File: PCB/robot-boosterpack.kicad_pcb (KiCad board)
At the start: 2 copper layers, 60 x 100 mm, 61 parts, among them IC1 DRV8833, IC2 TPS77033, IC3 TPS77050, IC4 LMR61428, J1 3.3V, J2 5V, J3 9V, M1 MOTOR, M2 MOTOR

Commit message: moved battery connector
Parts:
- moved CONN2 49.1 mm to (176.9, 131.8), turned to 90 degrees
- moved R5 4.41 mm to (195.4, 85.9), turned to 0 degrees
- moved J1 0.28 mm to (183.4, 144.4)
- moved J2 0.28 mm to (178.5, 144.4)
- moved D2 0.22 mm to (178.4, 152.2)
- moved R10 0.21 mm to (205.8, 106.7)
- moved D3 0.20 mm to (173.5, 152.2)
- moved D1 0.10 mm to (183.4, 152.2)
- moved R16 0.07 mm to (183.4, 149.1)
- moved R17 0.06 mm to (178.4, 149.1)
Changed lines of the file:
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@@
   )
   (module SM0603 (layer F.Cu)
-    (at 173.435 149.125 90)
+    (at 173.4 149.1 90)
     (attr smd)
     (fp_text reference R18 (at 0 0 90) (layer F.SilkS)
@@
   )
   (module SM0603 (layer B.Cu)
-    (at 205.75 106.5 270)
+    (at 205.8 106.7 270)
     (attr smd)
     (fp_text reference R10 (at 0 0 270) (layer B.SilkS)
@@
   )
   (module SM0603 (layer F.Cu)
-    (at 183.467 149.125 90)
+    (at 183.4 149.1 90)
     (attr smd)
     (fp_text reference R16 (at 0 0 90) (layer F.SilkS)
@@
   )
   (module SM0603 (layer F.Cu)
-    (at 178.451 149.125 90)
+    (at 178.4 149.1 90)
     (attr smd)
     (fp_text reference R17 (at 0 0 90) (layer F.SilkS)
@@
   )
   (module SM0603 (layer B.Cu)
-    (at 199.25 83.75 180)
-    (attr smd)
-    (fp_text reference R5 (at 0 0 180) (layer B.SilkS)
-      (effects (font (size 0.508 0.4572) (thickness 0.1143)) (justify mirror))
-    )
-    (fp_text value 22k (at 0 0 180) (layer B.SilkS) hide
-      (effects (font (size 0.508 0.4572) (thickness 0.1143)) (justify mirror))
-    )
-    (fp_line (start -1.143 0.635) (end 1.143 0.635) (layer B.SilkS) (width 0.127))
-    (fp_line (start 1.143 0.635) (end 1.143 -0.635) (layer B.SilkS) (width 0.127))
-    (fp_line (start 1.143 -0.635) (end -1.143 -0.635) (layer B.SilkS) (width 0.127))
-    (fp_line (start -1.143 -0.635) (end -1.143 0.635) (layer B.SilkS) (width 0.127))
-    (pad 1 smd rect (at -0.762 0 180) (size 0.635 1.143)
+    (at 195.4 85.9)
+    (attr smd)
+    (fp_text reference R5 (at 0 0) (layer B.SilkS)
+      (effects (font (size 0.508 0.4572) (thickness 0.1143)) (justify mirror))
+    )
+    (fp_text value 22k (at 0 0) (layer B.SilkS) hide
+      (effects (font (size 0.508 0.4572) (thickness 0.1143)) (justify mirror))
+    )
+    (fp_line (start -1.143 0.635) (end 1.143 0.635) (layer B.SilkS) (width 0.127))
+    (fp_line (start 1.143 0.635) (end 1.143 -0.635) (layer B.SilkS) (width 0.127))
+    (fp_line (start 1.143 -0.635) (end -1.143 -0.635) (layer B.SilkS) (width 0.127))
+    (fp_line (start -1.143 -0.635) (end -1.143 0.635) (layer B.SilkS) (width 0.127))
+    (pad 1 smd rect (at -0.762 0) (size 0.635 1.143)
       (layers B.Cu B.Paste B.Mask)
       (net 1 +3.3V)
     )
-    (pad 2 smd rect (at 0.762 0 180) (size 0.635 1.143)
+    (pad 2 smd rect (at 0.762 0) (size 0.635 1.143)
       (layers B.Cu B.Paste B.Mask)
       (net 24 N-0000021)
@@
   )
   (module PIN_ARRAY_3X1 (layer F.Cu)
-    (at 173.435 143.125 90)
+    (at 173.4 143.1 90)
     (descr "Connecteur 3 pins")
     (tags "CONN DEV")
@@
   )
   (module PIN_ARRAY_2X1 (layer F.Cu)
-    (at 178.451 144.125 90)
+    (at 178.5 144.4 90)
     (descr "Connecteurs 2 pins")
     (tags "CONN DEV")
@@
   )
   (module PIN_ARRAY_2X1 (layer F.Cu)
-    (at 226 131.5 270)
+    (at 176.9 131.8 90)
     (descr "Connecteurs 2 pins")
     (tags "CONN DEV")
-    (fp_text reference CONN2 (at 0 -1.905 270) (layer F.SilkS) hide
+    (fp_text reference CONN2 (at 0 -1.905 90) (layer F.SilkS) hide
       (effects (font (size 0.762 0.762) (thickness 0.1524)))
     )
-    (fp_text value BATTERY (at 0 -1.905 270) (layer F.SilkS)
-      (effects (font (size 0.762 0.762) (thickness 0.1524)))
+    (fp_text value BATTERY (at 0 -2.2 90) (layer F.SilkS)
+      (effects (font (size 1.016 1.016) (thickness 0.1524)))
     )
     (fp_line (start -2.54 1.27) (end -2.54 -1.27) (layer F.SilkS) (width 0.1524))
@@
     (fp_line (start 2.54 -1.27) (end 2.54 1.27) (layer F.SilkS) (width 0.1524))
     (fp_line (start 2.54 1.27) (end -2.54 1.27) (layer F.SilkS) (width 0.1524))
-    (pad 1 thru_hole rect (at -1.27 0 270) (size 1.524 1.524) (drill 1.016)
+    (pad 1 thru_hole rect (at -1.27 0 90) (size 1.524 1.524) (drill 1.016)
       (layers *.Cu *.Mask F.SilkS)
       (net 4 +BATT)
     )
-    (pad 2 thru_hole circle (at 1.27 0 270) (size 1.524 1.524) (drill 1.016)
+    (pad 2 thru_hole circle (at 1.27 0 90) (size 1.524 1.524) (drill 1.016)
       (layers *.Cu *.Mask F.SilkS)
       (net 16 GND)
@@
   )
   (module PIN_ARRAY_2X1 (layer F.Cu)
-    (at 183.467 144.125 90)
+    (at 183.4 144.4 90)
     (descr "Connecteurs 2 pins")
     (tags "CONN DEV")
@@
   )
   (module LED-0603 (layer F.Cu)
-    (at 183.467 152.125 270)
+    (at 183.4 152.2 270)
     (descr "LED 0603 smd package")
     (tags "LED led 0603 SMD smd SMT smt smdled SMDLED smtled SMTLED")
@@
   )
   (module LED-0603 (layer F.Cu)
-    (at 178.5 152 270)
+    (at 178.4 152.2 270)
     (descr "LED 0603 smd package")
     (tags "LED led 0603 SMD smd SMT smt smdled SMDLED smtled SMTLED")
@@
   )
   (module LED-0603 (layer F.Cu)
-    (at 173.5 152 270)
+    (at 173.5 152.2 270)
     (descr "LED 0603 smd package")
     (tags "LED led 0603 SMD smd SMT smt smdled SMDLED smtled SMTLED")

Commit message: initial bad routing
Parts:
- moved R1 8.20 mm to (178.0, 157.5), turned to 270 degrees
- moved R12 6.95 mm to (212.5, 157.0), turned to 270 degrees
- moved R6 6.95 mm to (194.5, 157.0), turned to 270 degrees
- moved D4 1.92 mm to (210.5, 125.0)
- moved R22 1.58 mm to (207.0, 121.0)
- moved IR1 1.50 mm to (174.5, 157.0)
- moved IR5 1.50 mm to (225.5, 157.0)
- moved R14 1.50 mm to (225.5, 151.0)
- moved R15 1.50 mm to (225.5, 153.0)
- moved R4 1.50 mm to (174.5, 153.0)
- moved R11 0.50 mm to (196.5, 157.0)
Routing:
- net GND: track 0.00 -> 303.6 mm, vias 0 -> 7
- net +3.3V: track 0.00 -> 196.7 mm, vias 0 -> 6
- net +5V: track 0.00 -> 153.2 mm, vias 0 -> 2
- net +9V: track 0.00 -> 113.9 mm, vias 0 -> 4
- net /IR5: track 0.00 -> 88.0 mm, vias 0 -> 1
- net /IR4: track 0.00 -> 87.2 mm, vias 0 -> 2
- net /IR3: track 0.00 -> 74.4 mm, vias 0 -> 6
- net /IR2: track 0.00 -> 69.3 mm, vias 0 -> 5
- net /IR1: track 0.00 -> 58.5 mm
- net /Distance: track 0.00 -> 57.8 mm, vias 0 -> 2
- net N-0000027: track 0.00 -> 52.4 mm, vias 0 -> 2
- net N-0000025: track 0.00 -> 49.3 mm, vias 0 -> 2
- net /Servo: track 0.00 -> 46.2 mm
- net N-0000034: track 0.00 -> 45.1 mm, vias 0 -> 2
- net /Left_Motor_1: track 0.00 -> 44.3 mm, vias 0 -> 1
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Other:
- net class Power added: clearance 0.254, trace_width 0.58, via_dia 0.889, via_drill 0.635

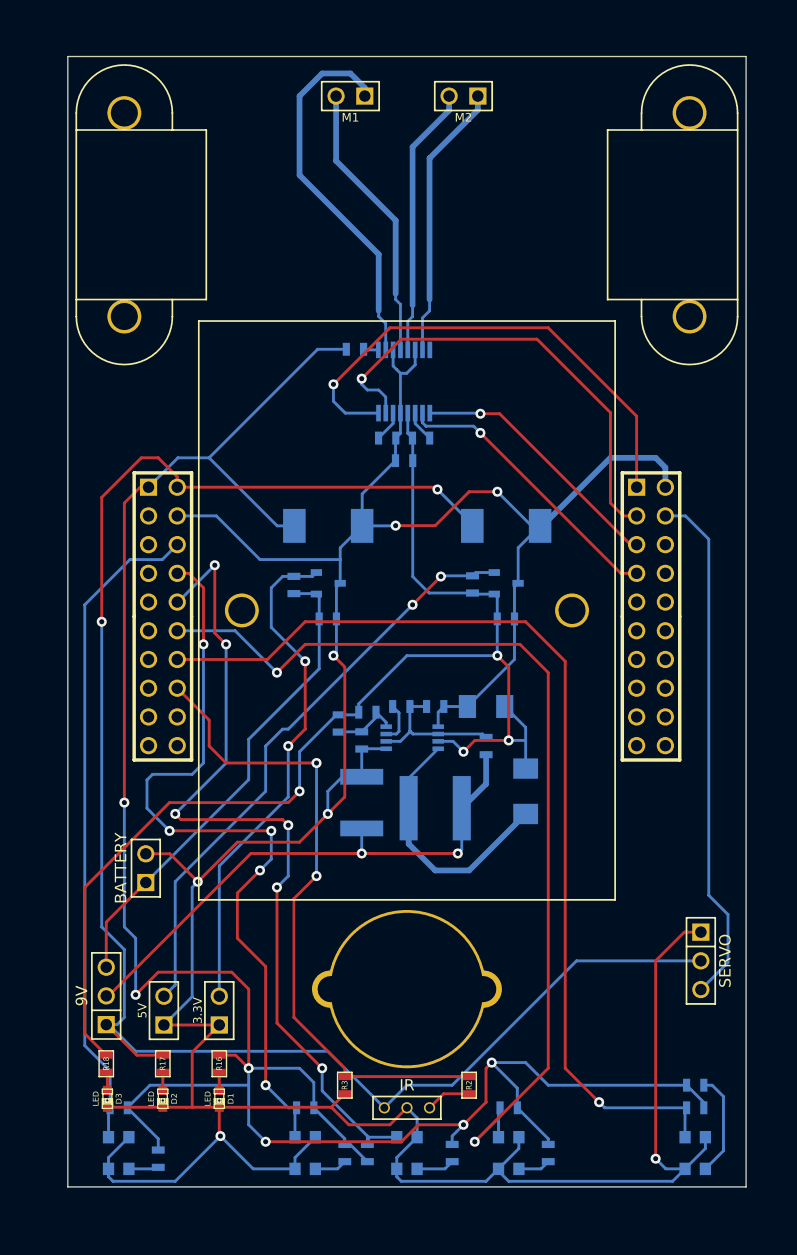
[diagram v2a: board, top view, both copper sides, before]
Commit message: finished basic routing, expanded trace width
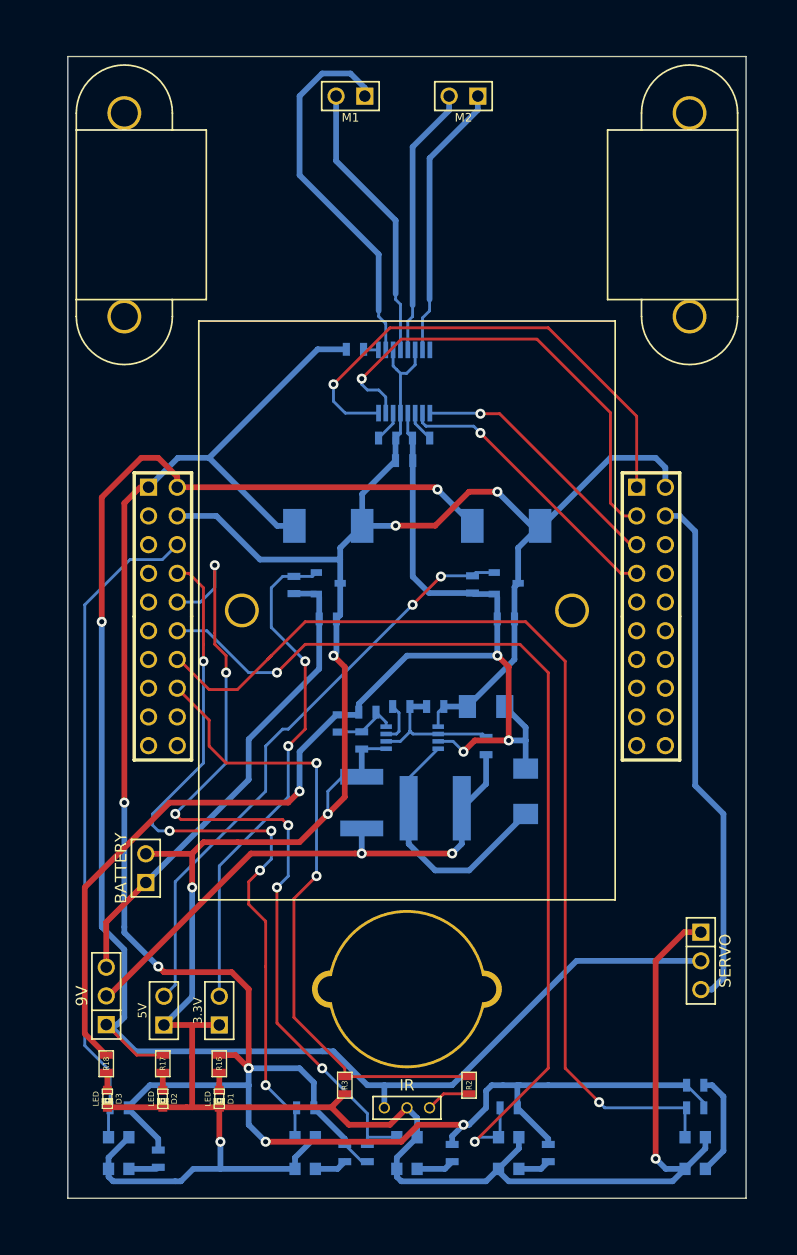
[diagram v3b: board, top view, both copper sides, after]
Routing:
- net +3.3V: track 196.7 -> 187.1 mm, vias 6 -> 5
- net /IR2: track 69.3 -> 66.6 mm
- net /IR5: track 88.0 -> 90.7 mm
- net /IR4: track 87.2 -> 85.7 mm
- net /IR3: track 74.4 -> 75.8 mm
- net N-0000025: track 49.3 -> 48.0 mm
- net +5V: track 153.2 -> 154.0 mm
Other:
- board size 60 x 100 mm -> 60 x 101 mm

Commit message: fixed IR sensor being backwards
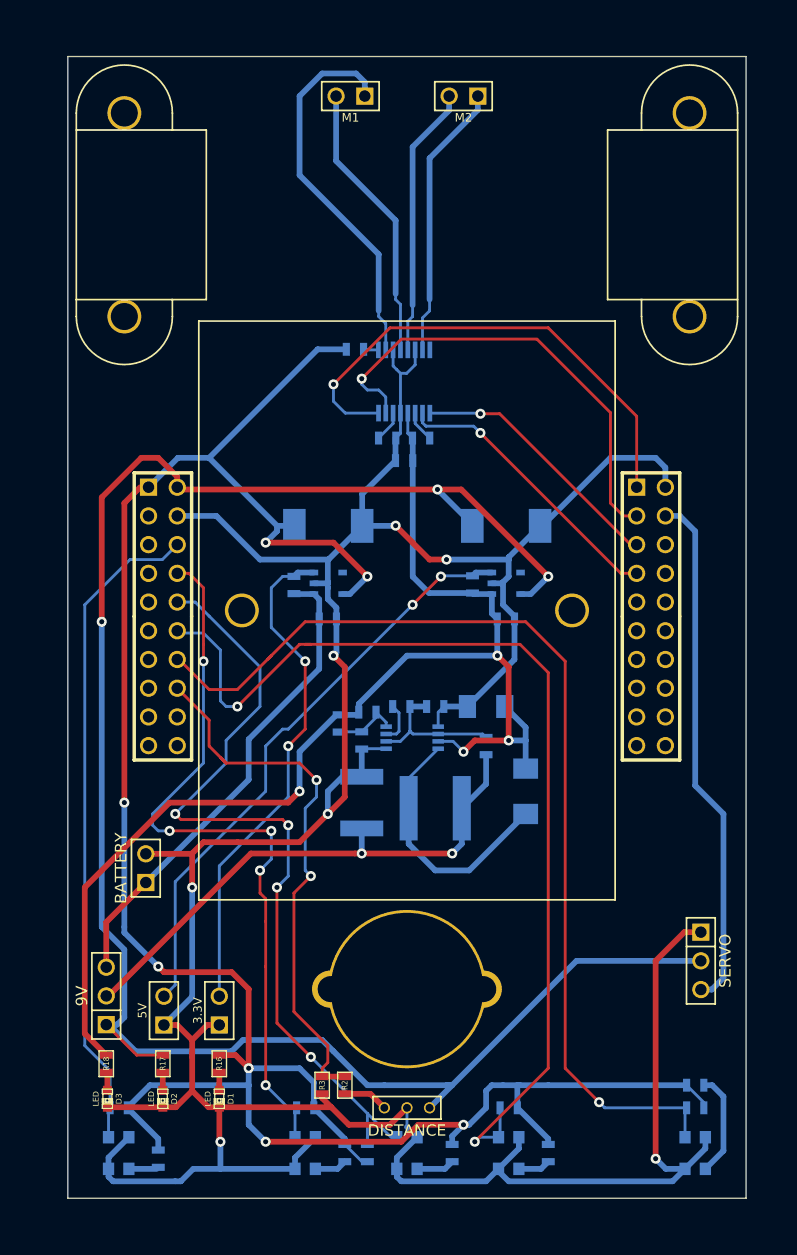
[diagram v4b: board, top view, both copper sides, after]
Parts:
- CONN3: value IR -> DISTANCE
- IC2, IC3: footprint sot23 -> SOT23-5
- moved R2 11.0 mm to (194.5, 151.0)
- moved CONN3 4.00 mm to (200.0, 155.0), turned to 180 degrees
- moved R3 2.00 mm to (192.5, 151.0)
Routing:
- net +5V: track 154.0 -> 172.1 mm, vias 2 -> 3
- net +3.3V: track 187.1 -> 202.1 mm, vias 5 -> 7
- net /Distance: track 57.8 -> 49.4 mm
- net /IR4: track 85.7 -> 91.4 mm
- net /IR3: track 75.8 -> 72.4 mm, vias 6 -> 4
- net GND: track 303.8 -> 301.8 mm
- net N-0000059: track 34.5 -> 35.5 mm
- net /IR2: track 66.6 -> 65.8 mm

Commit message: added ground planes
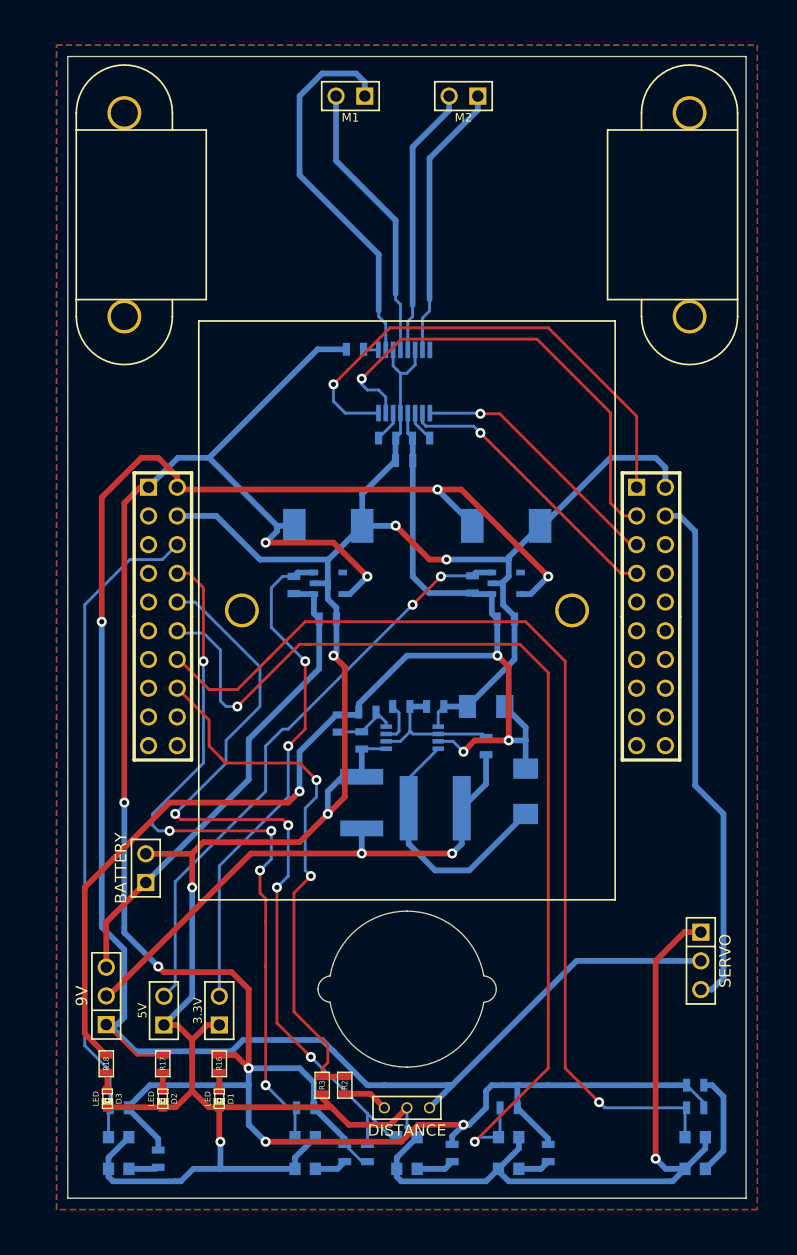
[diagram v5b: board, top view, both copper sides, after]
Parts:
- removed 3/8" Pololu Caster: VAL**, 0.375_Pololu_Caster
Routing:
- added copper zone on B.Cu, net GND
- added copper zone on F.Cu, net GND
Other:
- outline, holes or cut-outs redrawn
- board text added: "CUTOUT"
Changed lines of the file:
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@@
     (area 142.000002 36.650001 254 168.7)
     (thickness 1.6)
-    (drawings 18)
+    (drawings 28)
     (tracks 563)
     (zones 0)
-    (modules 61)
+    (modules 60)
     (nets 40)
   )
@@
   )
   (setup
-    (last_trace_width 0.508)
+    (last_trace_width 0.254)
     (user_trace_width 0.508)
     (user_trace_width 0.762)
@@
     (pad_to_mask_clearance 0)
     (aux_axis_origin 0 0)
-    (visible_elements 7FFFFFFF)
+    (visible_elements 7FFFFBFF)
     (pcbplotparams
-      (layerselection 3178497)
+      (layerselection 284196865)
       (usegerberextensions true)
       (excludeedgelayer true)
@@
       (outputformat 1)
       (mirror false)
-      (drillshape 1)
+      (drillshape 0)
       (scaleselection 1)
-      (outputdirectory ../../../../Desktop/))
+      (outputdirectory "../../../../Desktop/New folder/"))
   )
   (net 0 "")
@@
     )
   )
-  (module 0.375_Pololu_Caster (layer F.Cu)
-    (at 200 142.5)
-    (fp_text reference "3/8\" Pololu Caster" (at -0.1 0.5) (layer F.SilkS) hide
-      (effects (font (size 1 1) (thickness 0.15)))
-    )
-    (fp_text value VAL** (at 0.1 3.9) (layer F.SilkS) hide
-      (effects (font (size 1 1) (thickness 0.15)))
-    )
-    (pad "" np_thru_hole circle (at -6.75 0) (size 3.3 3.3) (drill 2.3)
-      (layers *.Cu *.Mask F.SilkS)
-    )
-    (pad "" np_thru_hole circle (at 6.75 0) (size 3.3 3.3) (drill 2.3)
-      (layers *.Cu *.Mask F.SilkS)
-    )
-    (pad "" np_thru_hole circle (at 0 0) (size 14 14) (drill 13.5)
-      (layers *.Cu *.Mask F.SilkS)
-    )
-  )
   (module NR6028T100M (layer B.Cu)
     (at 202.5 126.5 180)
@@
     )
   )
+  (gr_text "CUTOUT\n" (at 200 142.5) (layer Edge.Cuts)
+    (effects (font (size 1.5 1.5) (thickness 0.3)))
+  )
+  (gr_arc (start 206.731 142.5) (end 207.9 142.5) (angle 85) (layer Edge.Cuts) (width 0.1))
+  (gr_arc (start 206.731 142.5) (end 206.731 142.5) (angle -90) (layer Edge.Cuts) (width 0.1))
+  (gr_arc (start 193.3 142.5) (end 192.131 142.5) (angle -85) (layer Edge.Cuts) (width 0.1))
+  (gr_arc (start 193.3 142.5) (end 192.131 142.5) (angle 85) (layer Edge.Cuts) (width 0.1))
+  (gr_arc (start 200 142.5) (end 200 149.4) (angle -80.3) (layer Edge.Cuts) (width 0.1))
+  (gr_arc (start 200 142.5) (end 200 135.6) (angle -80.3) (layer Edge.Cuts) (width 0.1))
+  (gr_arc (start 200 142.5) (end 200 149.4) (angle 80.3) (layer Edge.Cuts) (width 0.1))
+  (gr_arc (start 206.731 142.5) (end 207.9 142.5) (angle -85) (layer Edge.Cuts) (width 0.1))
+  (gr_arc (start 200 142.5) (end 200 135.6) (angle 80.3) (layer Edge.Cuts) (width 0.1))
   (dimension 30 (width 0.3) (layer Cmts.User)
     (gr_text "30.000 mm" (at 185.000001 38.150001) (layer Cmts.User)
@@
   (segment (start 194 118.238) (end 195.5 118.238) (width 0.508) (layer B.Cu) (net 3))
   (segment (start 195.5 118.238) (end 195.738 118) (width 0.254) (layer B.Cu) (net 3))
-  (segment (start 192.238 109.75) (end 192.238 108.0205) (width 0.508) (layer B.Cu) (net 4))
-  (segment (start 192.238 108.0205) (end 191.77 107.5525) (width 0.508) (layer B.Cu) (net 4))
+  (segment (start 191.77 107.5525) (end 191.77 109.282) (width 0.508) (layer B.Cu) (net 4))
+  (segment (start 191.77 109.282) (end 192.238 109.75) (width 0.508) (layer B.Cu) (net 4))
   (segment (start 191.77 107.5525) (end 190.0405 107.5525) (width 0.508) (layer B.Cu) (net 4))
   (segment (start 190.0405 107.5525) (end 190 107.512) (width 0.508) (layer B.Cu) (net 4))
@@
   (segment (start 173.4 136.57) (end 176.9 133.07) (width 0.508) (layer F.Cu) (net 4))
   (segment (start 192.238 109.75) (end 192.238 114.162) (width 0.508) (layer B.Cu) (net 4))
+  (segment (start 186 123.97) (end 176.9 133.07) (width 0.508) (layer B.Cu) (net 4))
+  (segment (start 186 120.4) (end 186 123.97) (width 0.508) (layer B.Cu) (net 4))
   (segment (start 192.238 114.162) (end 186 120.4) (width 0.508) (layer B.Cu) (net 4))
-  (segment (start 186 120.4) (end 186 123.97) (width 0.508) (layer B.Cu) (net 4))
-  (segment (start 186 123.97) (end 176.9 133.07) (width 0.508) (layer B.Cu) (net 4))
   (segment (start 192.5 150.238) (end 192.5 149.5) (width 0.254) (layer F.Cu) (net 5))
   (segment (start 190.5 122.5) (end 184 122.5) (width 0.254) (layer F.Cu) (net 5))
@@
   (segment (start 228 141.5) (end 228 127) (width 0.508) (layer B.Cu) (net 15))
   (segment (start 226.96 142.54) (end 228 141.5) (width 0.508) (layer B.Cu) (net 15))
-  (segment (start 193.762 109.75) (end 193.762 112.738) (width 0.508) (layer B.Cu) (net 16) (status 400000))
+  (segment (start 193.762 109.75) (end 193.762 112.738) (width 0.508) (layer B.Cu) (net 16))
   (via (at 193.5 113) (size 0.889) (layers F.Cu B.Cu) (net 16))
   (segment (start 193.5 113) (end 194.5 114) (width 0.508) (layer F.Cu) (net 16))
@@
   (segment (start 199 81) (end 199 80) (width 0.254) (layer B.Cu) (net 36))
   (segment (start 199.42488 81.92488) (end 199 81.5) (width 0.254) (layer B.Cu) (net 36))
-  (segment (start 196.27 63.5) (end 196.27 62.27) (width 0.508) (layer B.Cu) (net 37) (status 400000))
+  (segment (start 196.27 63.5) (end 196.27 62.27) (width 0.508) (layer B.Cu) (net 37))
   (segment (start 197.5 77.5) (end 197.5 82.5) (width 0.508) (layer B.Cu) (net 37))
   (segment (start 190.5 70.5) (end 197.5 77.5) (width 0.508) (layer B.Cu) (net 37))
@@
   (segment (start 191.9 158.4) (end 193.862 158.4) (width 0.508) (layer B.Cu) (net 39))
   (segment (start 193.862 158.4) (end 194.5 157.762) (width 0.508) (layer B.Cu) (net 39))
+  (zone (net 16) (net_name GND) (layer F.Cu) (hatch edge 0.508)
+    (connect_pads (clearance 0.508))
+    (min_thickness 0.254)
+    (fill (arc_segments 16) (thermal_gap 0.508) (thermal_bridge_width 0.508))
+    (polygon
+      (pts
+        (xy 231 162) (xy 169 162) (xy 169 59) (xy 231 59)
+      )
+    )
+  )
+  (zone (net 16) (net_name GND) (layer B.Cu) (hatch edge 0.508)
+    (connect_pads (clearance 0.508))
+    (min_thickness 0.254)
+    (fill (arc_segments 16) (thermal_gap 0.508) (thermal_bridge_width 0.508))
+    (polygon
+      (pts
+        (xy 231 162) (xy 169 162) (xy 169 59) (xy 231 59)
+      )
+    )
+  )
 )

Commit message: logo and gerbers to send to fab
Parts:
- added G***: LOGO, LOGO, B.Cu at (200.0, 74.0)
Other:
- rule trace_min: 0.254 -> 0.1524
- rule via_min_size: 0.889 -> 0.3302
- board text added: "+"
- board text added: "-"
- board text added: "5V"
- board text added: "BATT"
- board text added: "CUT OUT"
- board text added: "GND"
- board text added: "SIG"
- board text removed: "CUTOUT"
